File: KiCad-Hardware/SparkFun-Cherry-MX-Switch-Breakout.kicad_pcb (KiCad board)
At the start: 2 copper layers, 19.1 x 19 mm, 16 parts

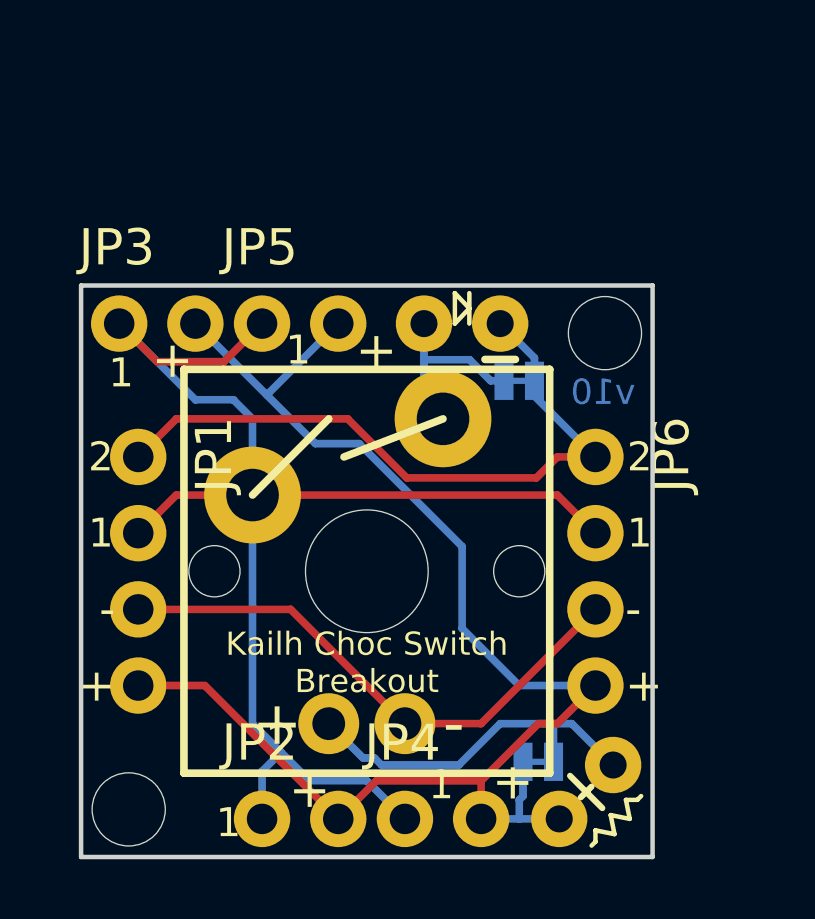
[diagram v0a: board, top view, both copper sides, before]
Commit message: First pass at a Kailh Choc breakout PCB
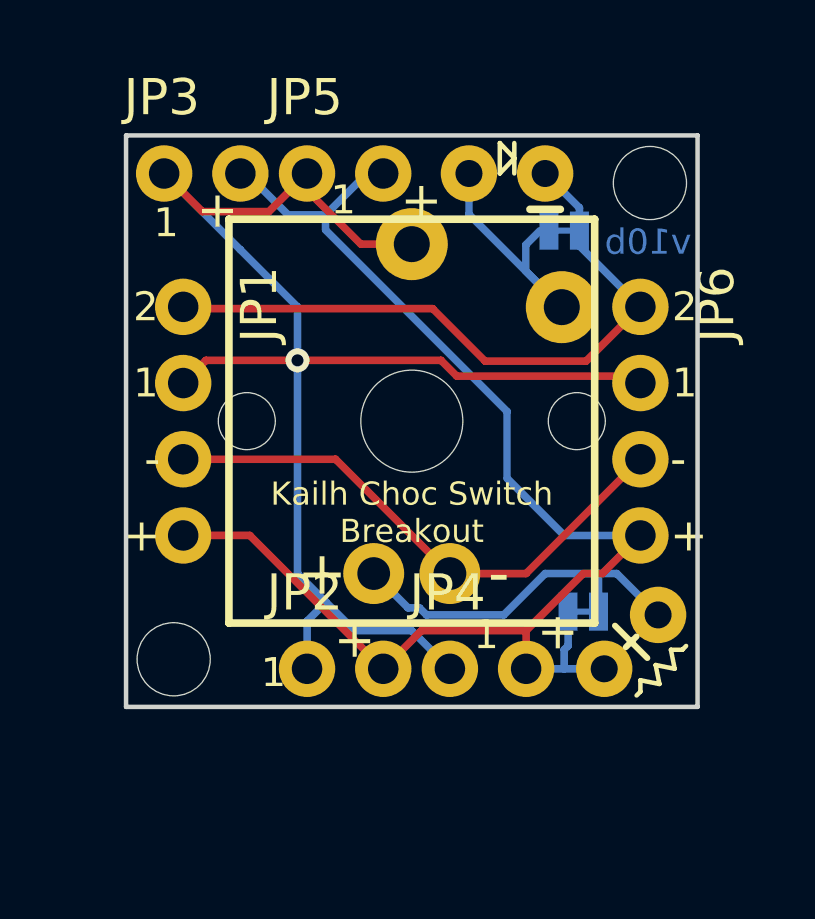
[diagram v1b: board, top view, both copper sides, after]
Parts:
- moved JP4 5.22 mm to (151.3, 108.3)
- moved JP1 5.22 mm to (142.4, 96.2)
- moved JP2 5.22 mm to (146.5, 108.3)
- moved JP6 5.22 mm to (157.6, 96.2)
- moved R1 5.22 mm to (156.4, 108.3)
- moved S1 5.22 mm to (150.0, 100.0)
- moved SJ1 5.22 mm to (155.7, 106.3)
- moved STANDOFF1 5.22 mm to (157.9, 92.1)
- moved STANDOFF2 5.22 mm to (142.1, 107.9)
- moved D1 5.22 mm to (153.2, 91.7)
- moved LOGO1 5.22 mm to (144.5, 106.3)
- moved SJ2 5.22 mm to (155.1, 93.7)
- moved JP3 5.22 mm to (141.7, 91.7)
- moved JP5 5.22 mm to (146.5, 91.7)
- moved LOGO2 5.22 mm to (153.8, 99.9)
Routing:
- net /SWITCH1: track 46.9 -> 50.5 mm, vias 0 -> 1
- net Net-(D1-PadA): track 6.39 -> 8.98 mm
- net /LEDA: track 48.1 -> 47.2 mm
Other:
- board size 19.1 x 19 mm -> 19.1 x 19.1 mm
- board text added: "v10b"
- board text removed: "v10"

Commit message: Commit of triplet version
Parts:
- added D1: DNP, SparkFun-Cherry-MX-Switch-Breakout:DIODE-PTH-0.1, F.Cu at (191.3, 91.7)
- added D1: DNP, SparkFun-Cherry-MX-Switch-Breakout:DIODE-PTH-0.1, F.Cu at (172.2, 91.7)
- added JP2: M021X02_NO_SILK, SparkFun-Cherry-MX-Switch-Breakout:1X02_NO_SILK, F.Cu at (184.6, 108.3)
- added JP2: M021X02_NO_SILK, SparkFun-Cherry-MX-Switch-Breakout:1X02_NO_SILK, F.Cu at (165.6, 108.3)
- added JP3: M021X02_NO_SILK, SparkFun-Cherry-MX-Switch-Breakout:1X02_NO_SILK, F.Cu at (179.8, 91.7)
- added JP3: M021X02_NO_SILK, SparkFun-Cherry-MX-Switch-Breakout:1X02_NO_SILK, F.Cu at (160.8, 91.7)
- added JP4: M021X02_NO_SILK, SparkFun-Cherry-MX-Switch-Breakout:1X02_NO_SILK, F.Cu at (189.4, 108.3)
- added JP4: M021X02_NO_SILK, SparkFun-Cherry-MX-Switch-Breakout:1X02_NO_SILK, F.Cu at (170.3, 108.3)
- added JP5: M021X02_NO_SILK, SparkFun-Cherry-MX-Switch-Breakout:1X02_NO_SILK, F.Cu at (184.6, 91.7)
- added JP5: M021X02_NO_SILK, SparkFun-Cherry-MX-Switch-Breakout:1X02_NO_SILK, F.Cu at (165.6, 91.7)
- added LOGO1: OSHW-LOGOS, SparkFun-Cherry-MX-Switch-Breakout:OSHW-LOGO-S, B.Cu at (182.6, 106.3)
- added LOGO1: OSHW-LOGOS, SparkFun-Cherry-MX-Switch-Breakout:OSHW-LOGO-S, B.Cu at (163.5, 106.3)
- added LOGO2: SFE_LOGO_FLAME.1_INCH, SparkFun-Cherry-MX-Switch-Breakout:SFE_LOGO_FLAME_.1, B.Cu at (191.9, 99.9)
- added LOGO2: SFE_LOGO_FLAME.1_INCH, SparkFun-Cherry-MX-Switch-Breakout:SFE_LOGO_FLAME_.1, B.Cu at (172.9, 99.9)
- added R1: DNP, SparkFun-Cherry-MX-Switch-Breakout:AXIAL-0.1, F.Cu at (194.5, 108.3)
- added R1: DNP, SparkFun-Cherry-MX-Switch-Breakout:AXIAL-0.1, F.Cu at (175.5, 108.3)
- added S1: CHERRY-MX-LED, SparkFun-Cherry-MX-Switch-Breakout:CHERRY-MX-LED, F.Cu at (188.1, 100.0)
- added S1: CHERRY-MX-LED, SparkFun-Cherry-MX-Switch-Breakout:CHERRY-MX-LED, F.Cu at (169.1, 100.0)
- added SJ1: JUMPER-PAD-2-NC_BY_TRACENO_SILK, SparkFun-Cherry-MX-Switch-Breakout:PAD-JUMPER-2-NC_BY_TRACE_NO_SILK, B.Cu at (193.8, 106.3)
- added SJ1: JUMPER-PAD-2-NC_BY_TRACENO_SILK, SparkFun-Cherry-MX-Switch-Breakout:PAD-JUMPER-2-NC_BY_TRACE_NO_SILK, B.Cu at (174.8, 106.3)
- added SJ2: JUMPER-PAD-2-NC_BY_TRACENO_SILK, SparkFun-Cherry-MX-Switch-Breakout:PAD-JUMPER-2-NC_BY_TRACE_NO_SILK, B.Cu at (193.2, 93.7)
- added SJ2: JUMPER-PAD-2-NC_BY_TRACENO_SILK, SparkFun-Cherry-MX-Switch-Breakout:PAD-JUMPER-2-NC_BY_TRACE_NO_SILK, B.Cu at (174.1, 93.7)
- added STANDOFF2: STAND-OFF2-56, SparkFun-Cherry-MX-Switch-Breakout:STAND-OFF-2-56, F.Cu at (180.2, 107.9)
- added STANDOFF2: STAND-OFF2-56, SparkFun-Cherry-MX-Switch-Breakout:STAND-OFF-2-56, F.Cu at (161.1, 107.9)
- moved JP6 38.1 mm to (195.7, 96.2)
- moved STANDOFF1 38.1 mm to (196.0, 92.1)
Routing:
- net /SWITCH1: track 50.5 -> 158.8 mm, vias 1 -> 3
- net /LEDA: track 47.2 -> 149.2 mm, vias 0 -> 2
- net /SWITCH2: track 22.5 -> 75.2 mm, vias 0 -> 2
- net /LEDC: track 18.4 -> 62.8 mm
- net Net-(R1-PadP$2): track 12.5 -> 37.4 mm
- net Net-(D1-PadA): track 8.98 -> 26.9 mm
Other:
- board size 19.1 x 19.1 mm -> 57.2 x 19.1 mm
